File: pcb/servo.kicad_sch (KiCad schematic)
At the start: 1 part, among them J24 Conn_01x03_Pin

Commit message: Finish for revision 2 production
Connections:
- net +5V: now also J24.2 (Pin_2); no longer J24.3 (Pin_3)
- net SIG: now also J24.3 (Pin_3); no longer J24.2 (Pin_2)
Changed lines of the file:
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@@
 	(wire
 		(pts
-			(xy 81.28 55.88) (xy 81.28 58.42)
+			(xy 81.28 55.88) (xy 81.28 60.96)
 		)
 		(stroke
@@
 	(wire
 		(pts
-			(xy 81.28 58.42) (xy 83.82 58.42)
+			(xy 81.28 60.96) (xy 83.82 60.96)
 		)
 		(stroke
@@
 	(wire
 		(pts
-			(xy 81.28 60.96) (xy 83.82 60.96)
+			(xy 78.74 58.42) (xy 83.82 58.42)
 		)
 		(stroke
@@
 	(hierarchical_label "SIG"
 		(shape input)
-		(at 81.28 60.96 180)
+		(at 78.74 58.42 180)
 		(fields_autoplaced yes)
 		(effects
@@
 					(unit 1)
 				)
-				(path "/38b0a34b-2047-47f6-90d7-ccdf77e8e212/7e3f67f4-c7a7-4f15-a62c-4903c0d88b19/b34e6cdb-0429-4c8b-ab94-be7f1417c867"
-					(reference "#PWR0259")
-					(unit 1)
-				)
 				(path "/38b0a34b-2047-47f6-90d7-ccdf77e8e212/7e3f67f4-c7a7-4f15-a62c-4903c0d88b19/c43efd4d-e310-4bbf-b378-f4ca4f0e12c9"
 					(reference "#PWR0251")
@@
 					(unit 1)
 				)
-				(path "/38b0a34b-2047-47f6-90d7-ccdf77e8e212/7e3f67f4-c7a7-4f15-a62c-4903c0d88b19/b34e6cdb-0429-4c8b-ab94-be7f1417c867"
-					(reference "#PWR0260")
-					(unit 1)
-				)
 				(path "/38b0a34b-2047-47f6-90d7-ccdf77e8e212/7e3f67f4-c7a7-4f15-a62c-4903c0d88b19/c43efd4d-e310-4bbf-b378-f4ca4f0e12c9"
 					(reference "#PWR0252")
@@
 					(unit 1)
 				)
-				(path "/38b0a34b-2047-47f6-90d7-ccdf77e8e212/7e3f67f4-c7a7-4f15-a62c-4903c0d88b19/b34e6cdb-0429-4c8b-ab94-be7f1417c867"
-					(reference "J25")
-					(unit 1)
-				)

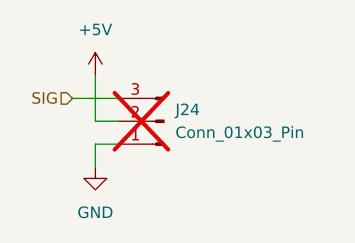
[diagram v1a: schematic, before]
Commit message: Fix encoder pull downs
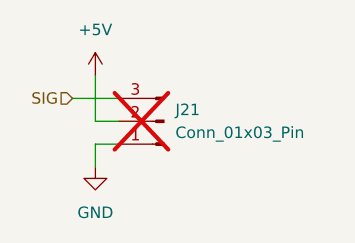
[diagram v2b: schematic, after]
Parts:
- renumbered J24 to J21
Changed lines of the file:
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@@
 (kicad_sch
-	(version 20231120)
+	(version 20250114)
 	(generator "eeschema")
-	(generator_version "8.0")
+	(generator_version "9.0")
 	(paper "A5")
 	(wire
@@
 		(shape input)
 		(at 78.74 58.42 180)
-		(fields_autoplaced yes)
 		(effects
 			(font
@@
 		(dnp no)
 		(fields_autoplaced yes)
-		(property "Reference" "#PWR0257"
+		(property "Reference" "#PWR0251"
 			(at 81.28 59.69 0)
 			(effects
@@
 		(dnp no)
 		(fields_autoplaced yes)
-		(property "Reference" "#PWR0258"
+		(property "Reference" "#PWR0252"
 			(at 81.28 72.39 0)
 			(effects
@@
 		(on_board yes)
 		(dnp yes)
-		(property "Reference" "J24"
+		(property "Reference" "J21"
 			(at 90.17 59.6899 0)
 			(effects
